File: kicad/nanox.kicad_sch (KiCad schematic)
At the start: 137 parts, among them P1 likely an ESD protection diod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, P2 likely an ESD protection diod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, P3 likely an ESD protection diod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, P4 likely an ESD protection diod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, P5 likely an ESD protection diod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, SW1 push button, left, SW2 push button, right, X1 ?, X10 TI TLV61046A boost converter 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, X2 unknown, marked 2GC, X3 unknown, marked 6, X4 ?, X5 ?, X6 ?, X7 ?, X8 ?, X9 unknown, marked P8W 26, Y1 crystal, likely the 32 MHz HSE

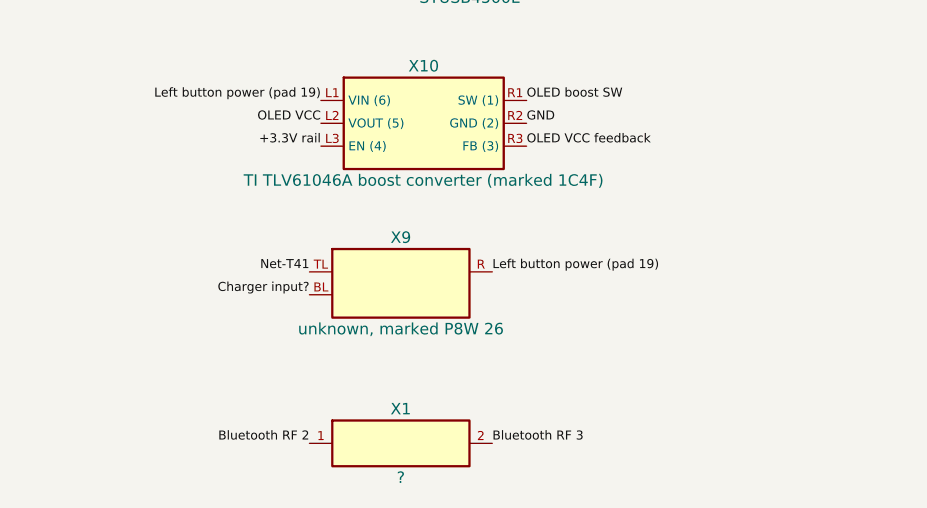
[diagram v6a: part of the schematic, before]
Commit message: Identify X9 as an NXP PMBZ5246B 16 V Zener diode
It was taken for a power switch. With its P8W 26 marking upright, its
cathode (pin 3) is on the supply that feeds the OLED boost converter, its
anode (pin 1) on the charger's input supply, and its unconnected pin 2
sits on battery +. Descriptions that called it a power switch or the
source of that supply are corrected. Connectivity is unchanged.

Co-Authored-By: Claude Opus 5.5 <noreply@anthropic.com>
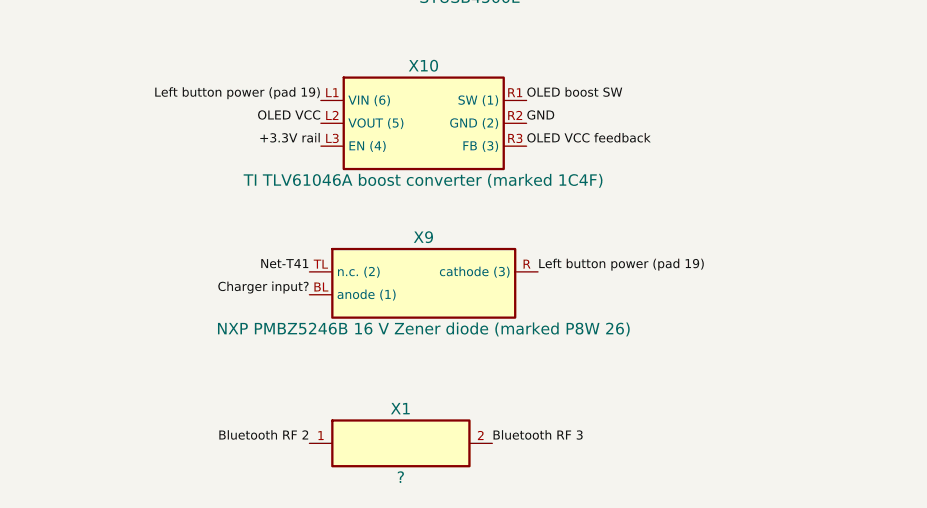
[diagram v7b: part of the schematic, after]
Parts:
- X9: value unknown, marked P8W 26 -> NXP PMBZ5246B 16 V Zener diode (marked P8W 26)
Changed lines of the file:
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@@
  (label "GND" (at 463.55 261.62 0) (effects (font (size 1.0 1.0)) (justify left bottom)))
  (label "OLED VCC feedback" (at 463.55 264.16 0) (effects (font (size 1.0 1.0)) (justify left bottom)))
- (symbol (lib_id "nanox:X9") (at 449.58 279.40 0) (unit 1) (in_bom yes) (on_board yes) (dnp no)
-  (property "Reference" "X9" (at 449.58 274.32 0) (effects (font (size 1.27 1.27))))
-  (property "Value" "unknown, marked P8W 26" (at 449.58 284.48 0) (effects (font (size 1.27 1.27))))
-  (property "Footprint" "" (at 449.58 279.40 0) (effects (font (size 1.27 1.27)) hide))
-  (property "Description" "3 terminals, SOT-23 style, ~1.3 x 2.9 mm body" (at 449.58 279.40 0) (effects (font (size 1.27 1.27)) hide))
+ (symbol (lib_id "nanox:X9") (at 452.12 279.40 0) (unit 1) (in_bom yes) (on_board yes) (dnp no)
+  (property "Reference" "X9" (at 452.12 274.32 0) (effects (font (size 1.27 1.27))))
+  (property "Value" "NXP PMBZ5246B 16 V Zener diode (marked P8W 26)" (at 452.12 284.48 0) (effects (font (size 1.27 1.27))))
+  (property "Footprint" "" (at 452.12 279.40 0) (effects (font (size 1.27 1.27)) hide))
+  (property "Description" "SOT-23, 2.9 x 1.3 mm" (at 452.12 279.40 0) (effects (font (size 1.27 1.27)) hide))
   (pin "TL")
   (pin "BL")
@@
  (label "Net-T41" (at 439.42 278.13 180) (effects (font (size 1.0 1.0)) (justify right bottom)))
  (label "Charger input?" (at 439.42 280.67 180) (effects (font (size 1.0 1.0)) (justify right bottom)))
- (label "Left button power (pad 19)" (at 459.74 278.13 0) (effects (font (size 1.0 1.0)) (justify left bottom)))
+ (label "Left button power (pad 19)" (at 464.82 278.13 0) (effects (font (size 1.0 1.0)) (justify left bottom)))
  (symbol (lib_id "nanox:X1") (at 449.58 297.18 0) (unit 1) (in_bom yes) (on_board yes) (dnp no)
   (property "Reference" "X1" (at 449.58 293.37 0) (effects (font (size 1.27 1.27))))

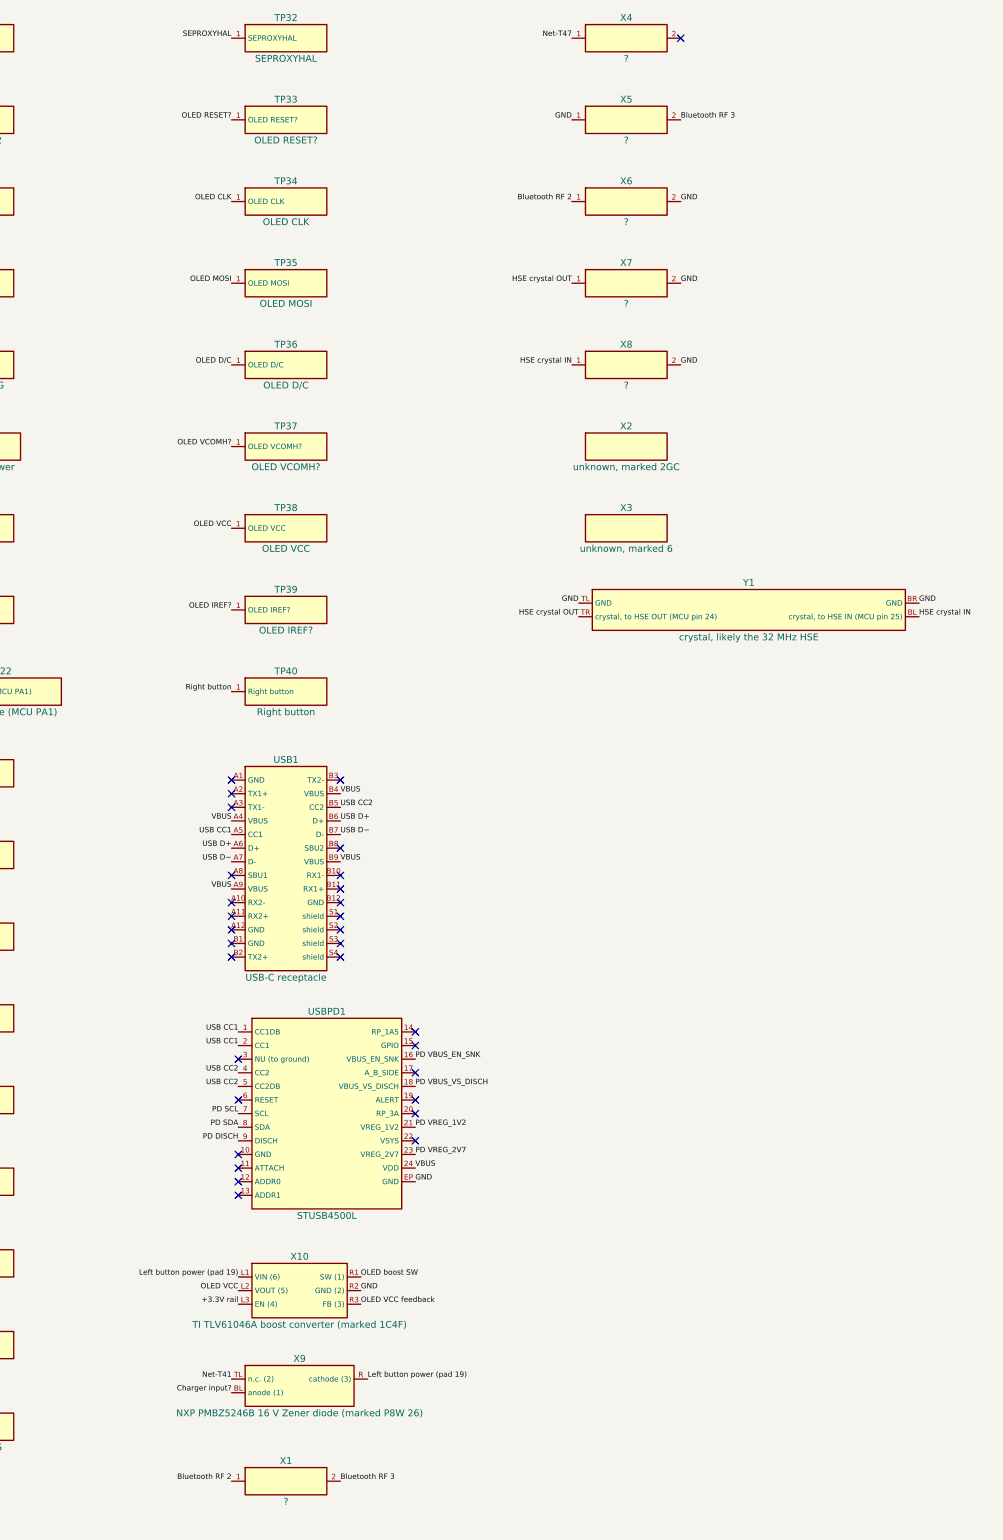
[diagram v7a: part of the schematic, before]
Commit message: Add X11, the 4-pad part marked AF between C9 and C8/C10
Three traces ended on it unconnected: the supply on the left button
(pad 19), VDDUSB (the MCU's USB supply, with C9-C12) and the net from MCU
PB3 and the charger input through R16/R29. Its fourth pad is ground,
joined to C10's ground pad, and carries the dot seen on the part. From
those nets it is likely a small LDO making VDDUSB, enabled by the MCU or
by USB power; not confirmed.

Co-Authored-By: Claude Opus 5.5 <noreply@anthropic.com>
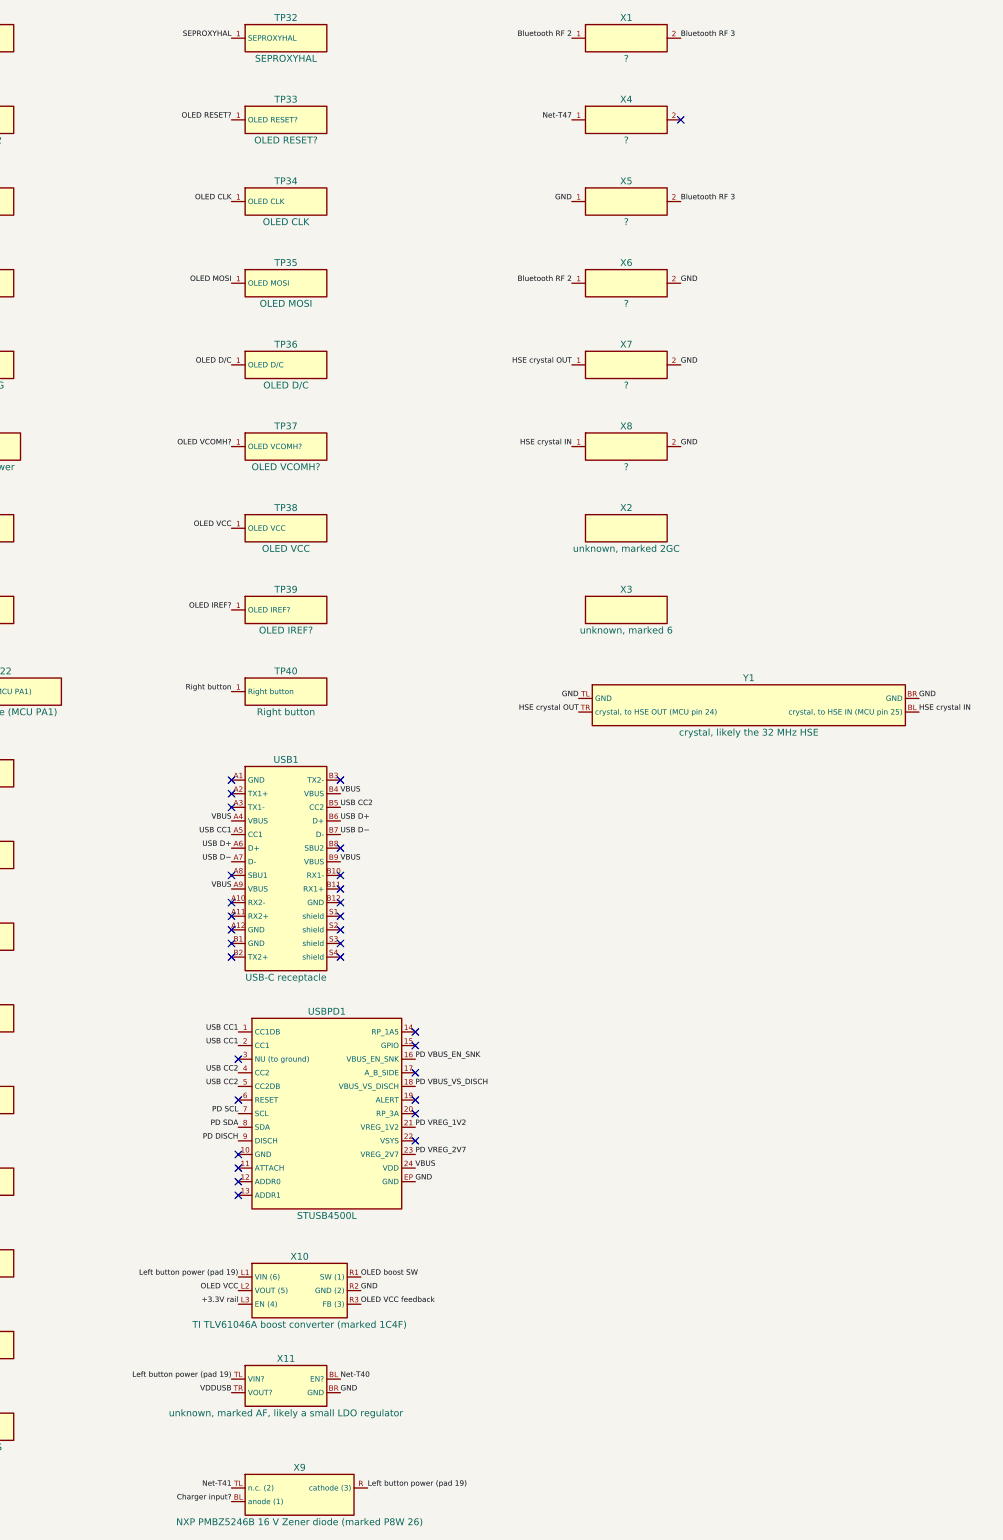
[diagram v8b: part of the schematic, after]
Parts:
- added X11: unknown, marked AF, likely a small LDO regulator, symbol nanox:X11
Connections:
- net GND: now also X11.BR (GND)
- net Left button power (pad 19): now also X11.TL (VIN?)
- net Net-T40: now also X11.BL (EN?)
- net VDDUSB: now also X11.TR (VOUT?)
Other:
- moved on the sheet: X1, X2, X3, X4, X5, X6, X7, X8, X9, Y1
